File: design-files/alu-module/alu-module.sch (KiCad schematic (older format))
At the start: 30 parts, among them U301 74HCT273, U302 74LS382A, U303 74HCT377, U304 74HCT245, U305 74HCT08, U306 74LS382A, U307 4002

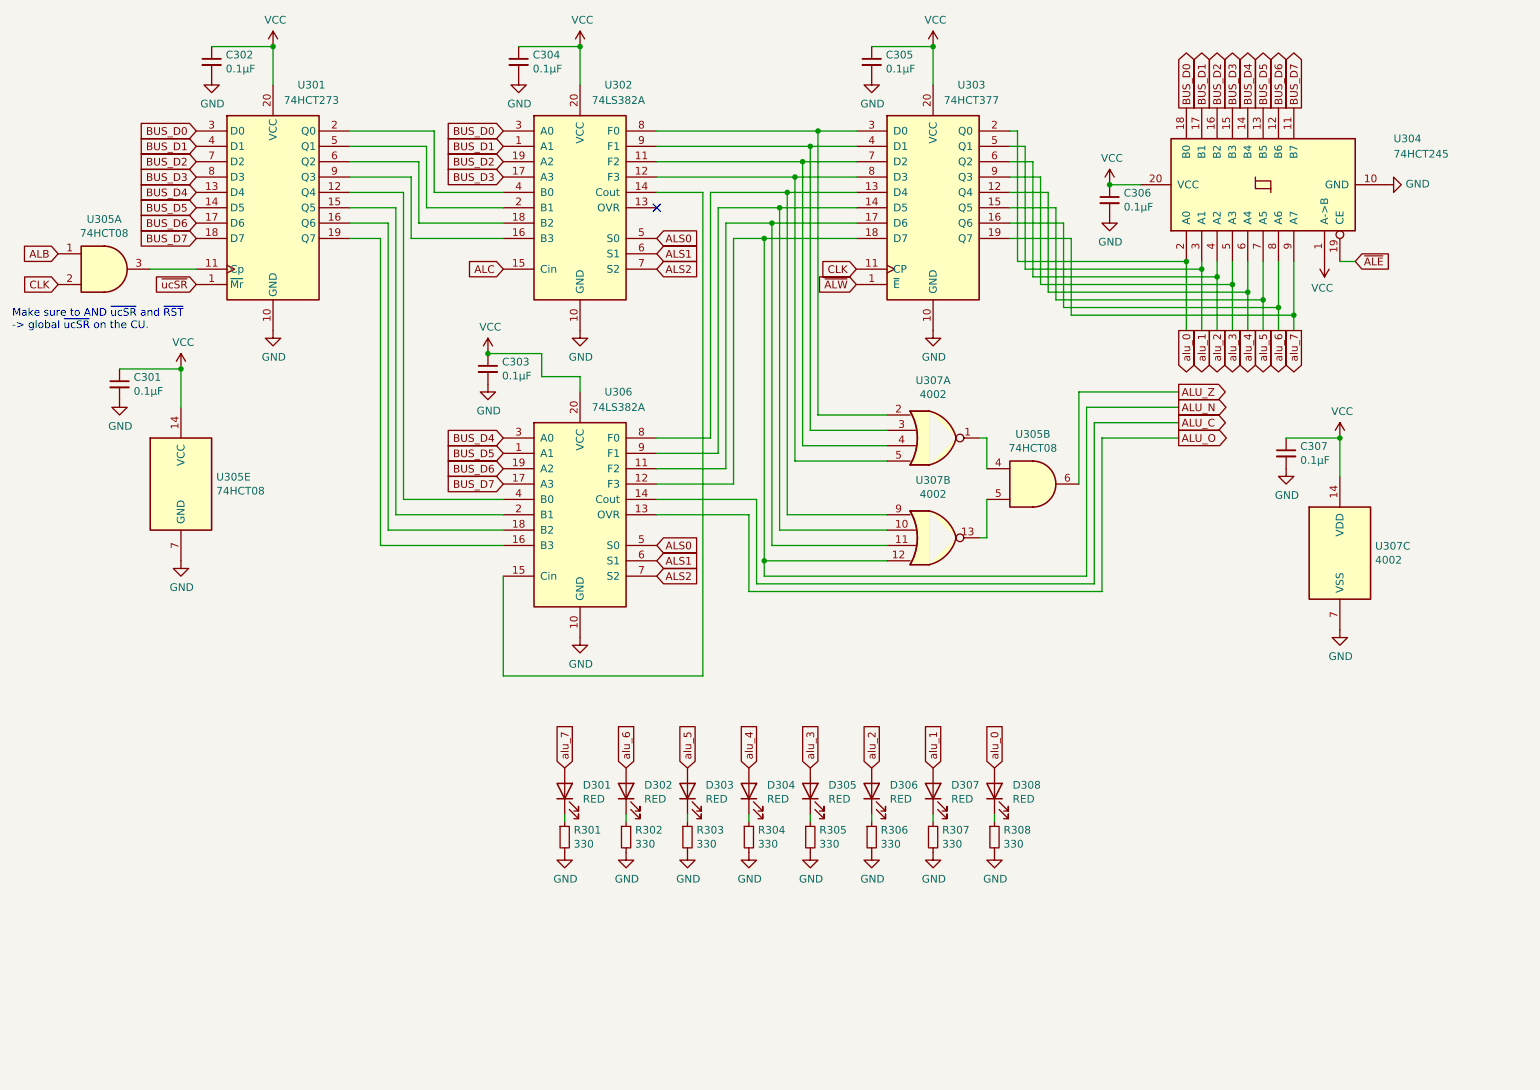
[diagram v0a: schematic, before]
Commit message: For ALU_B, don't use an AND gate with CLK to do the write-enable, as this could cause spurious rising-edges, and thus spurious loads into the register.  Use a pair of '157 muxes in front of the register intead. Change the ALB signal back to _ALB (active-low).
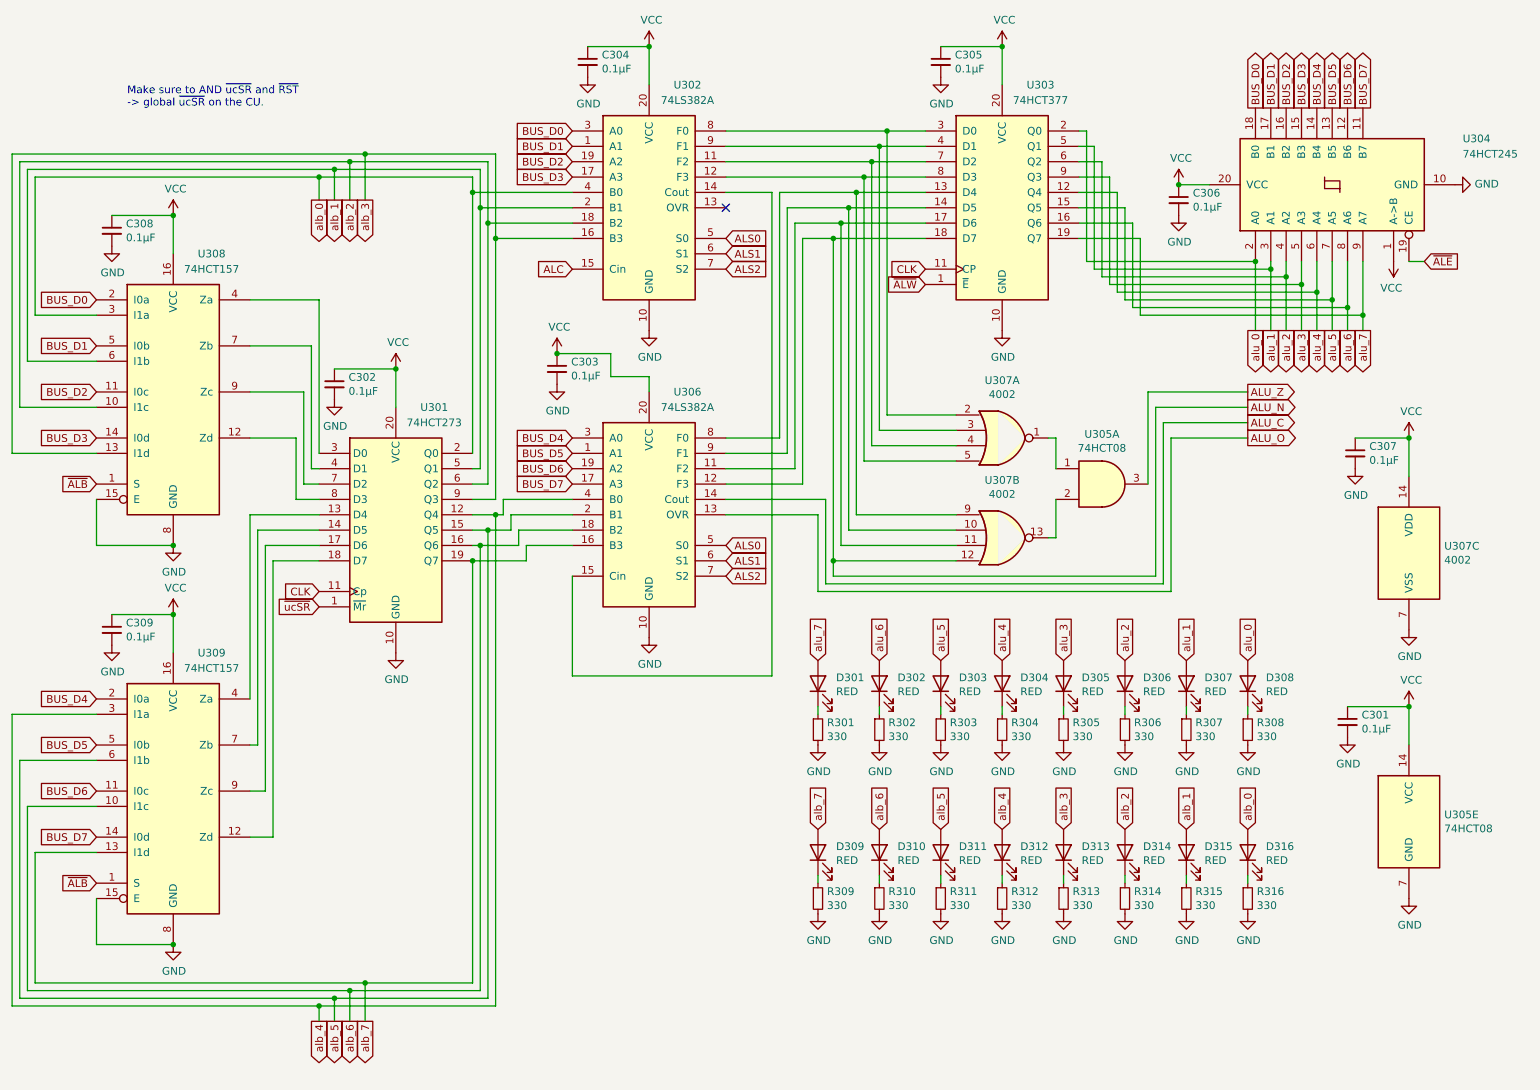
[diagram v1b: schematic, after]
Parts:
- removed unit 1 of U305
- added C308, C309: 0.1µF, Capacitor_THT:C_Radial_D6.3mm_H5.0mm_P2.50mm, symbol Device:C_Small
- added D309, D310, D311, D312, D313, D314, D315, D316: RED, LED_THT:LED_D5.0mm, symbol Device:LED
- added R309, R310, R311, R312, R313, R314, R315, R316: 330, Resistor_THT:R_Axial_DIN0204_L3.6mm_D1.6mm_P5.08mm_Horizontal, symbol Device:R_Small
- added U308, U309: 74HCT157, Package_DIP:DIP-16_W7.62mm_Socket, symbol 74xx:74LS157
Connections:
- net ALU_Z: now also U305.3; no longer U305.6
- net BUS_D0: now also U308.2 (I0a); no longer U301.3 (D0)
- net BUS_D1: now also U308.5 (I0b); no longer U301.4 (D1)
- net BUS_D2: now also U308.11 (I0c); no longer U301.7 (D2)
- net BUS_D3: now also U308.14 (I0d); no longer U301.8 (D3)
- net BUS_D4: now also U309.2 (I0a); no longer U301.13 (D4)
- net BUS_D5: now also U309.5 (I0b); no longer U301.14 (D5)
- net BUS_D6: now also U309.11 (I0c); no longer U301.17 (D6)
- net BUS_D7: now also U309.14 (I0d); no longer U301.18 (D7)
- net CLK: now also U301.11 (Cp)
- net GND: now also C308.2, C309.2, R309.2, R310.2, R311.2, R312.2, R313.2, R314.2, R315.2, R316.2, U308.15 (E), U308.8 (GND), U309.15 (E), U309.8 (GND)
- net VCC: now also C308.1, C309.1, U308.16 (VCC), U309.16 (VCC)
- net alb_4: now reaches U301.12 (Q4), U306.4 (B0)
- net alb_4: now also D312.2 (A), U309.3 (I1a)
- net alb_5: now reaches U301.15 (Q5), U306.2 (B1)
- net alb_5: now also D311.2 (A), U309.6 (I1b)
- net alb_6: now reaches U301.16 (Q6), U306.18 (B2)
- net alb_6: now also D310.2 (A), U309.10 (I1c)
- net alb_7: now reaches U301.19 (Q7), U306.16 (B3)
- net alb_7: now also D309.2 (A), U309.13 (I1d)
- net alb_0: now reaches U301.2 (Q0), U302.4 (B0)
- net alb_0: now also D316.2 (A), U308.3 (I1a)
- net alb_1: now reaches U301.5 (Q1), U302.2 (B1)
- net alb_1: now also D315.2 (A), U308.6 (I1b)
- net alb_2: now reaches U301.6 (Q2), U302.18 (B2)
- net alb_2: now also D314.2 (A), U308.10 (I1c)
- net alb_3: now reaches U301.9 (Q3), U302.16 (B3)
- net alb_3: now also D313.2 (A), U308.13 (I1d)
- net at U307.1: now also U305.1; no longer U305.4
- net at U307.13: now also U305.2; no longer U305.5
- new net: U301.8 (D3), U308.12 (Zd)
- new net: U301.3 (D0), U308.4 (Za)
- new net: U301.4 (D1), U308.7 (Zb)
- new net: U301.7 (D2), U308.9 (Zc)
- new net: U301.18 (D7), U309.12 (Zd)
- new net: U301.13 (D4), U309.4 (Za)
- new net: U301.14 (D5), U309.7 (Zb)
- new net: U301.17 (D6), U309.9 (Zc)
- new net: D309.1 (K), R309.1
- new net: D310.1 (K), R310.1
- new net: D311.1 (K), R311.1
- new net: D312.1 (K), R312.1
- new net: D313.1 (K), R313.1
- new net: D314.1 (K), R314.1
- new net: D315.1 (K), R315.1
- new net: D316.1 (K), R316.1
- new net ~ALB: U308.1 (S), U309.1 (S)
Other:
- moved on the sheet: C301, C302, C303, C304, C305, C306, C307, D301, D302, D303, D304, D305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

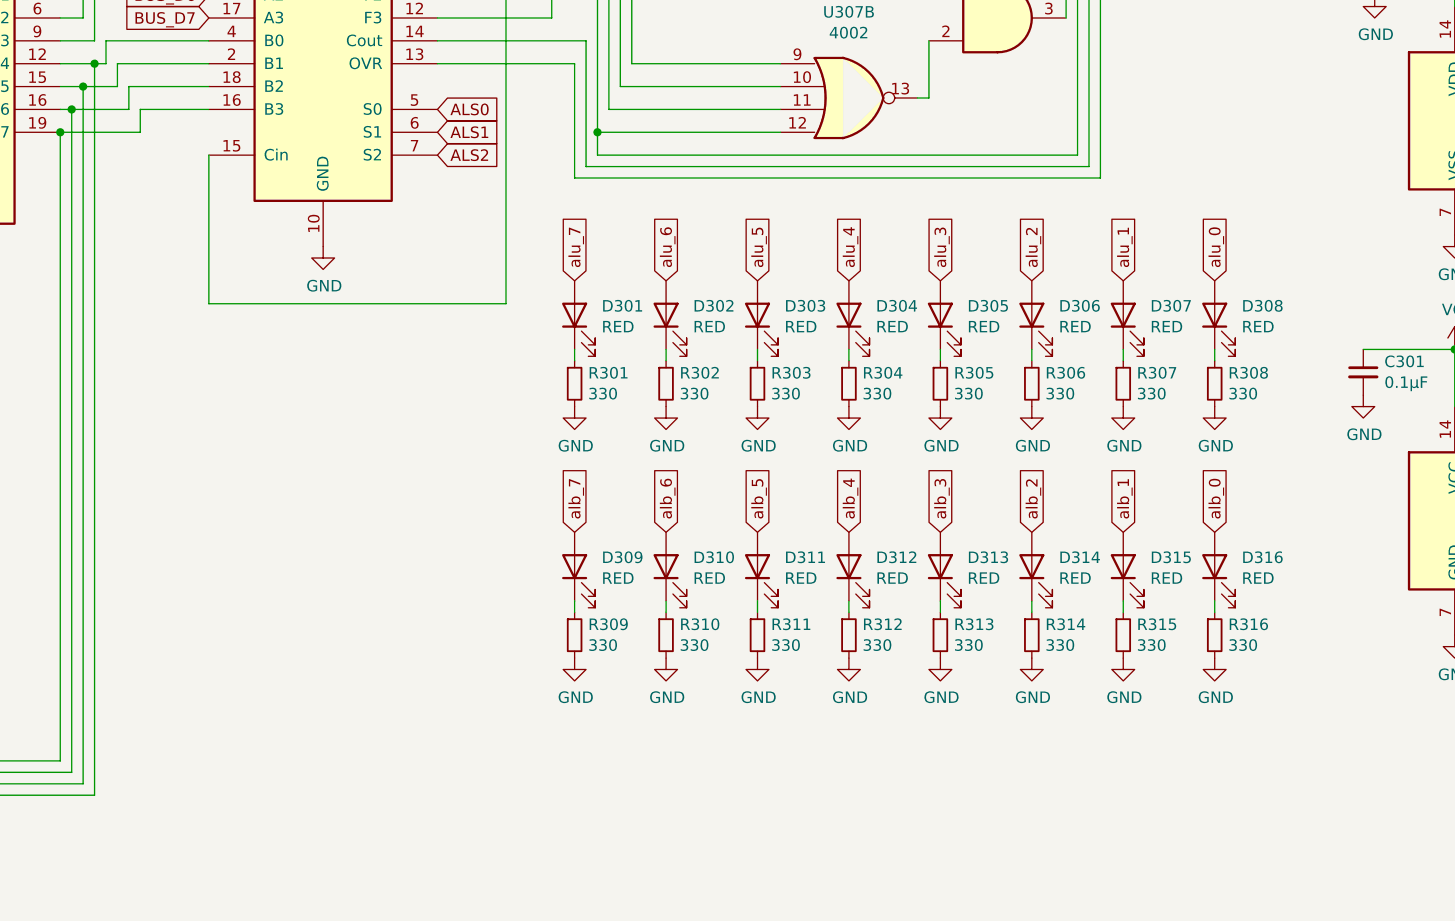
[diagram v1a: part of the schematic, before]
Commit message: Rework to use DIP resistor packs for the LEDs.
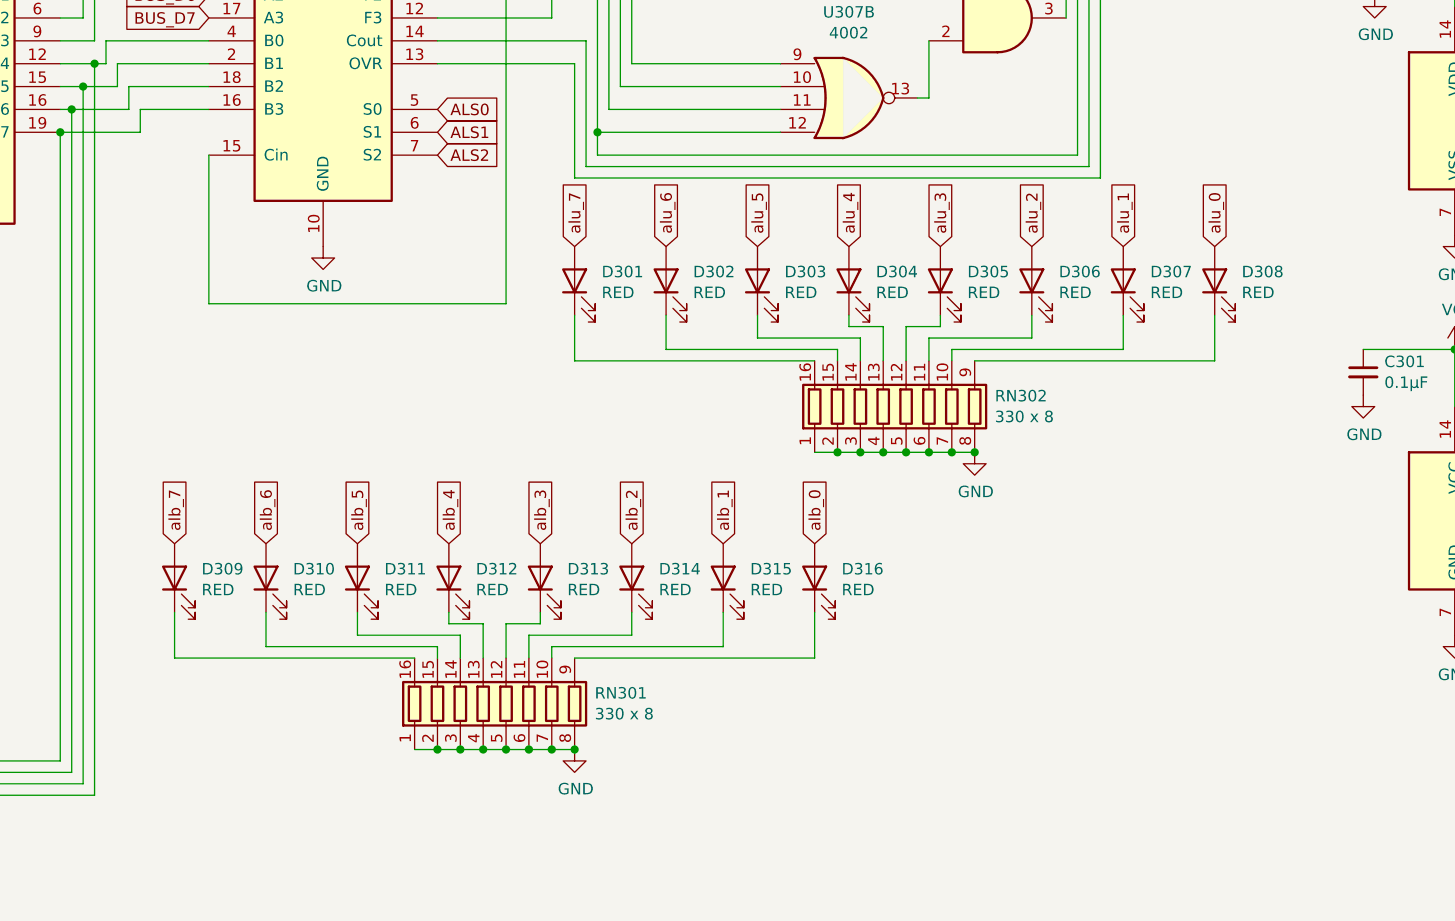
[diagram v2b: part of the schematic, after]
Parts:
- removed R301, R302, R303, R304, R305, R306, R307, R308, R309, R310, R311, R312, R313, R314, R315, R316: 330, Resistor_THT:R_Axial_DIN0204_L3.6mm_D1.6mm_P5.08mm_Horizontal, symbol Device:R_Small
- added RN301, RN302: 330 x 8, Package_DIP:DIP-16_W7.62mm_Socket, symbol Device:R_Pack08
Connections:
- net GND: now also RN301.1 (R1.1), RN301.2 (R2.1), RN301.3 (R3.1), RN301.4 (R4.1), RN301.5 (R5.1), RN301.6 (R6.1), RN301.7 (R7.1), RN301.8 (R8.1), RN302.1 (R1.1), RN302.2 (R2.1), RN302.3 (R3.1), RN302.4 (R4.1), RN302.5 (R5.1), RN302.6 (R6.1), RN302.7 (R7.1), RN302.8 (R8.1)
- net at D309.1 (K): now also RN301.16 (R1.2)
- net at D310.1 (K): now also RN301.15 (R2.2)
- net at D311.1 (K): now also RN301.14 (R3.2)
- net at D312.1 (K): now also RN301.13 (R4.2)
- net at D313.1 (K): now also RN301.12 (R5.2)
- net at D314.1 (K): now also RN301.11 (R6.2)
- net at D315.1 (K): now also RN301.10 (R7.2)
- net at D316.1 (K): now also RN301.9 (R8.2)
- net at D301.1 (K): now also RN302.16 (R1.2)
- net at D302.1 (K): now also RN302.15 (R2.2)
- net at D303.1 (K): now also RN302.14 (R3.2)
- net at D304.1 (K): now also RN302.13 (R4.2)
- net at D305.1 (K): now also RN302.12 (R5.2)
- net at D306.1 (K): now also RN302.11 (R6.2)
- net at D307.1 (K): now also RN302.10 (R7.2)
- net at D308.1 (K): now also RN302.9 (R8.2)
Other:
- moved on the sheet: D301, D302, D303, D304, D305, D306, D307, D308, D309, D310, D311, D312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
